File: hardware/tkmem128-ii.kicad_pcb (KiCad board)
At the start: 4 copper layers, 78.7 x 66 mm, 22 parts, among them J1 Barramento TK, U1 GAL20V8B, U2 74HCT273, U3 AS6C1008-55PCN, U4 27C256

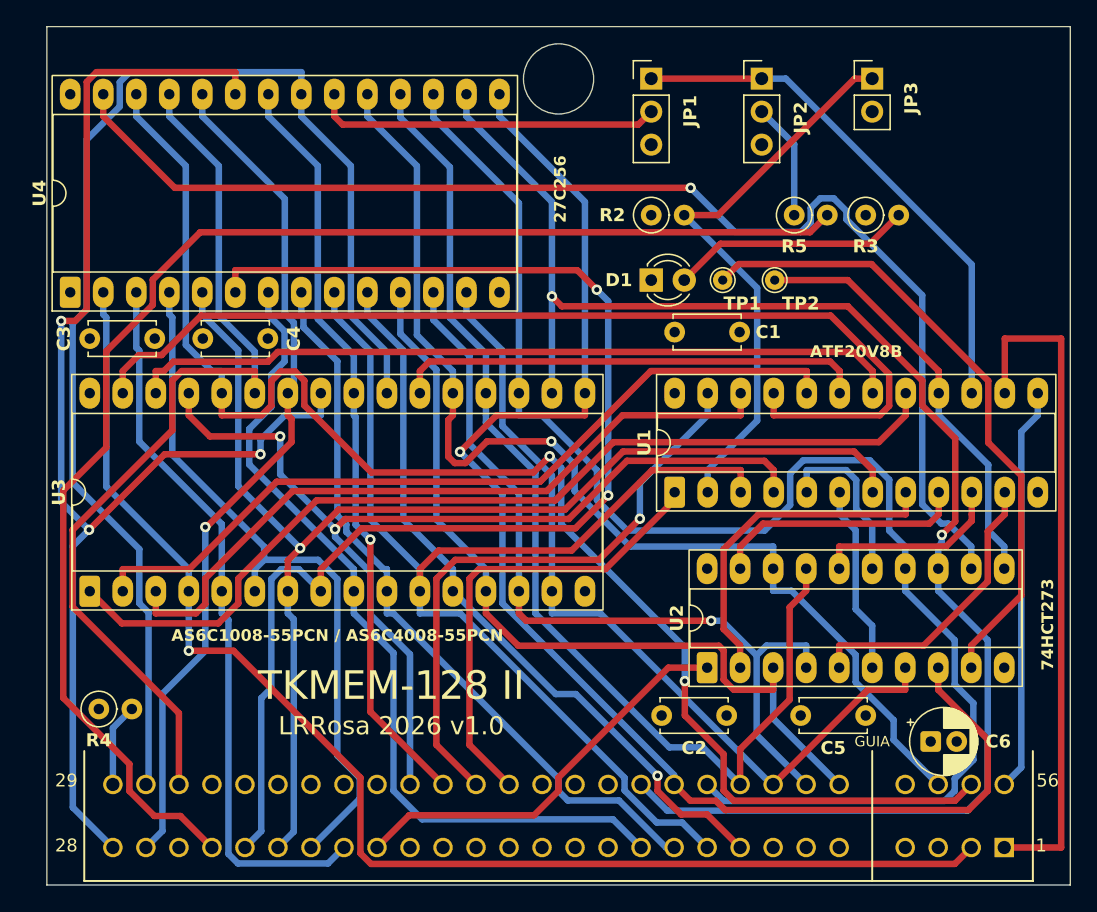
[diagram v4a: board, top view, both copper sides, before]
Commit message: Referencia de U4 de volta a placa, e C6 longe dos terminais de J1
A referencia de U4 estava em x = -0,57 — FORA da placa. Ela seguia a convencao
das outras (0,7 mm a esquerda do courtyard) e foi junto quando U4 recuou 1,5 mm
para abrir o furo da torre. Nada acusou: DRC nao reclama de serigrafia que sai
do contorno, ela simplesmente nao aparece no gerber. So se ve olhando o render.

A esquerda nao ha mais espaco (o courtyard de U4 comeca em 0,17), entao a
referencia passou para a direita, junto do nome do componente. E o `27C256`,
que estava a 3,05 mm do courtyard por heranca de antes do recuo, voltou para
1,25 mm. Lidos de baixo para cima saem como "U4 27C256".

C6 x J1: o corpo do capacitor (Ø5,10) terminava a **0,44 mm** dos terminais da
fileira de cima do conector. Nao e problema eletrico — cobre a cobre sao 1,81
mm — e sim de bancada: esses terminais atravessam a placa e sobram 3,18 mm do
lado dos componentes, que e onde a tira de expansao e soldada dos dois lados.
Soldar aquela fileira com uma lata de 5 mm a meio milimetro e ruim.

C6 subiu 0,70 mm: 1,13 mm ate o terminal e 1,11 mm ate o corpo do soquete de
U2. Nao exigiu rerotear — as duas ilhas de C6 sao +5V e GND, e nesta placa
alimentacao nao usa trilha nenhuma, cada ilha toca o plano interno direto.

0,70 e nao 0,80 porque a ilha 2 raspa numa diagonal de D3 a 45 graus, que se
aproxima 1/raiz(2) por milimetro de subida: com 0,80 dava 0,195 contra os 0,200
da regra, cinco microns. O script mede as trilhas vizinhas antes de gravar e
recusa — conferido com teste negativo.

DRC 0/0, os quatro conferidores OK.

Co-Authored-By: Claude Opus 5 <noreply@anthropic.com>
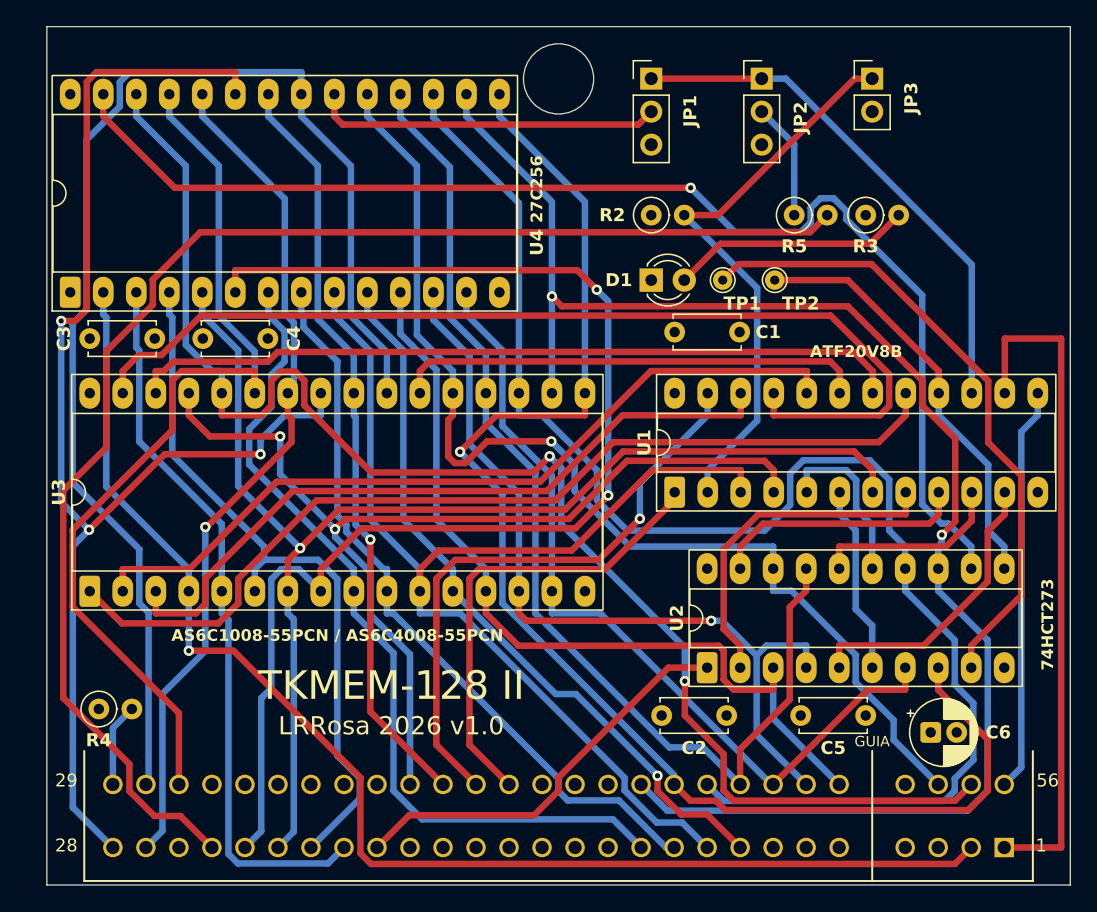
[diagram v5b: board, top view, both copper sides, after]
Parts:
- moved C6 0.70 mm to (68.0, 54.3)
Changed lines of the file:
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@@
 		(tags "THT DIP DIL PDIP 2.54mm 15.24mm 600mil Socket LongPads")
 		(property "Reference" "U4"
-			(at 7.62 -2.37 90)
+			(at 3.84 35.9 90)
 			(layer "F.SilkS")
 			(effects
@@
 	(footprint "CP_Radial_D5.0mm_P2.00mm"
 		(layer "F.Cu")
-		(at 68 55)
+		(at 68 54.3)
 		(descr "CP, Radial series, Radial, pin pitch=2.00mm, diameter=5mm, height=7mm, Electrolytic Capacitor")
 		(tags "CP Radial series Radial pin pitch 2.00mm diameter 5mm height 7mm Electrolytic Capacitor")
@@
 	)
 	(gr_text "27C256"
-		(at 39.5 12.5 90)
+		(at 37.7 12.5 90)
 		(layer "F.SilkS")
 		(effects
